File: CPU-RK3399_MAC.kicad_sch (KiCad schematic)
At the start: 15 parts, among them U1 RK3399

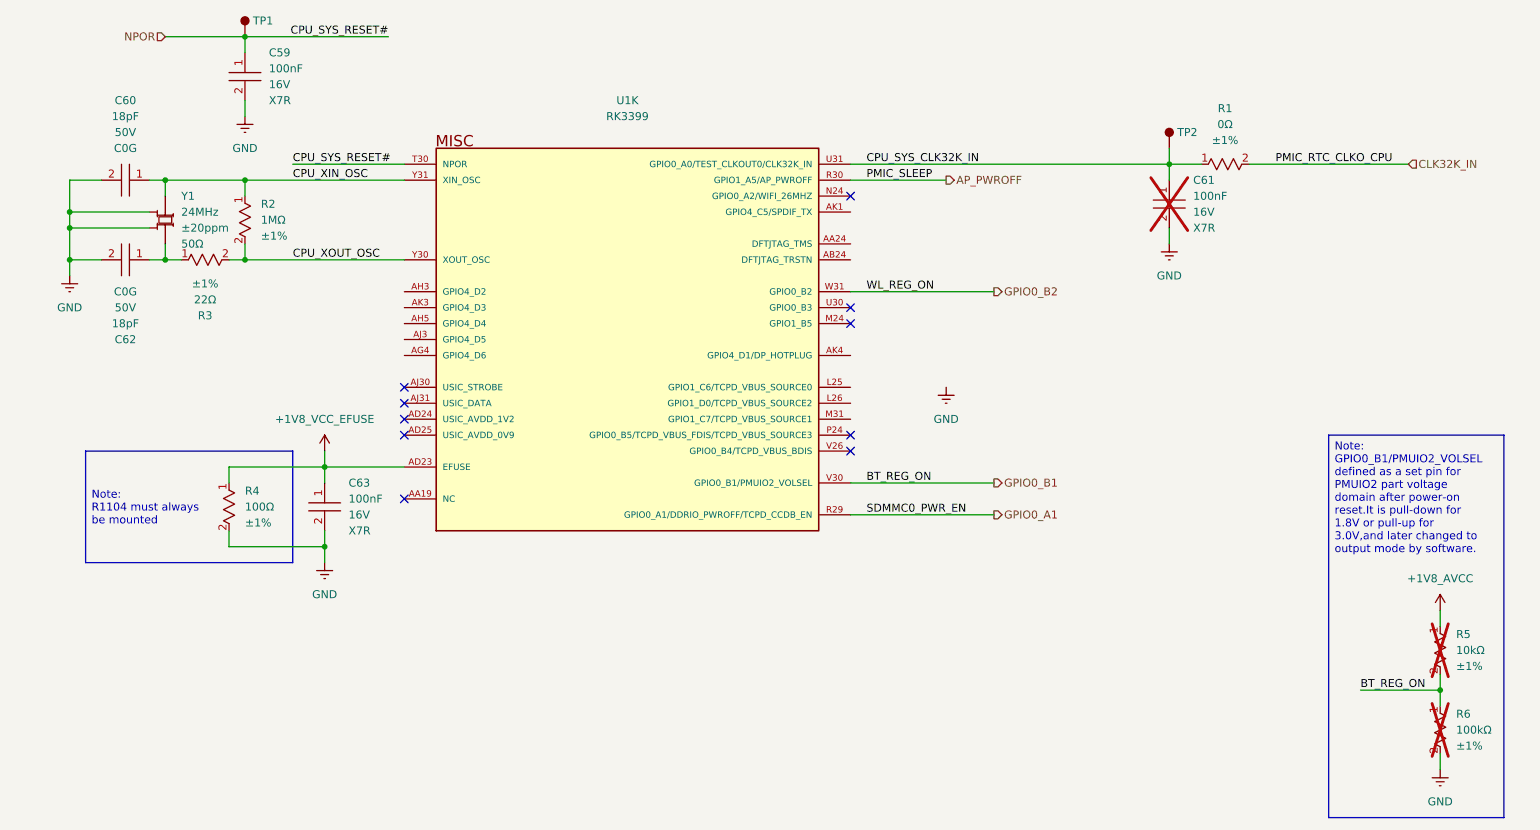
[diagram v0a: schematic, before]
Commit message: update schematic
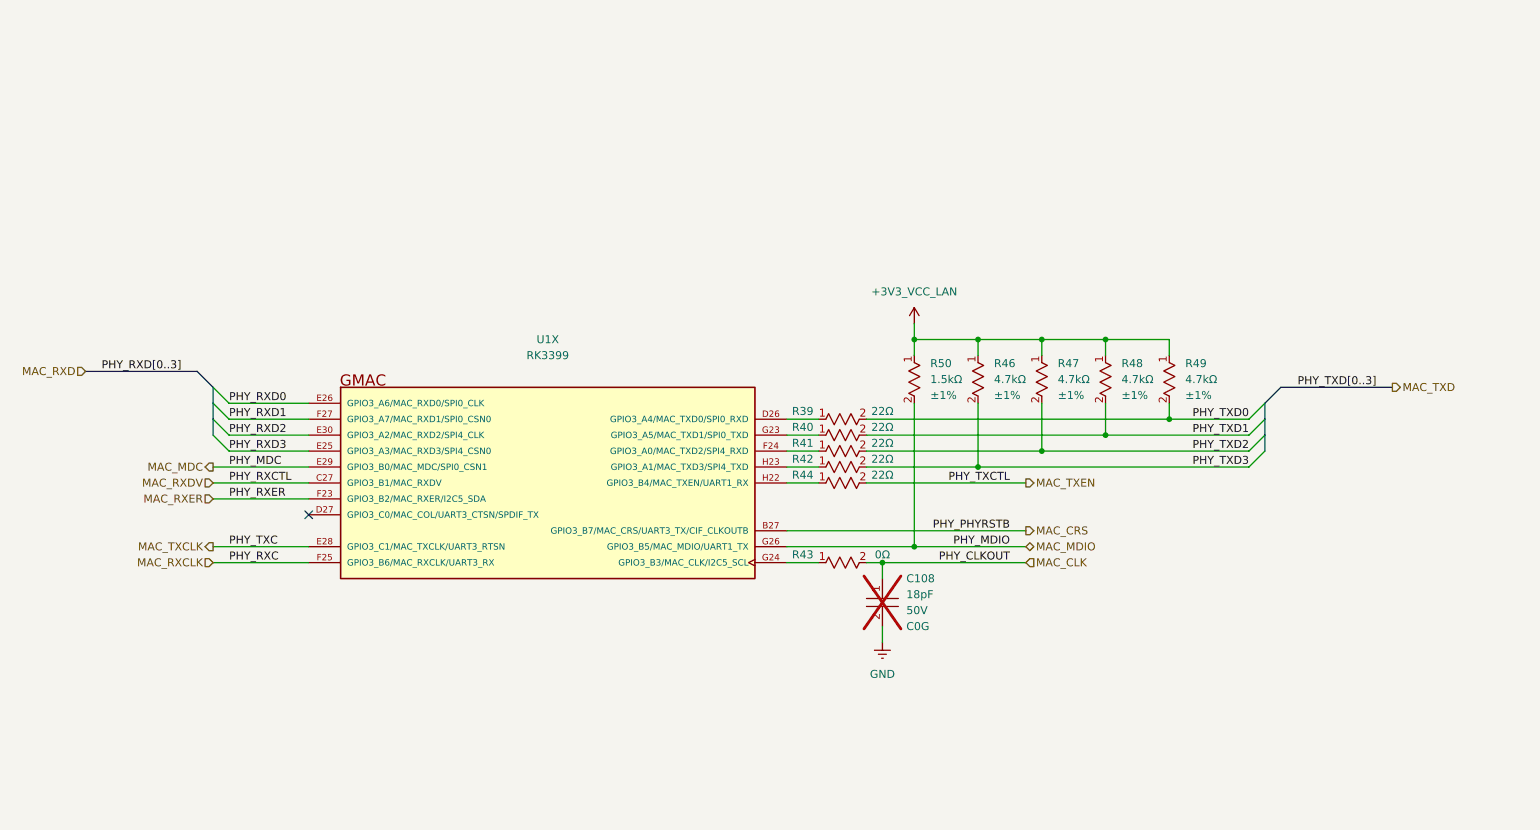
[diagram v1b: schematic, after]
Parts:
- removed C59, C61, C63: ~, footprints:CAPC1005X50N, symbol component_library:Capacitors/CL05B104KO5NNNC
- removed C60, C62: ~, footprints:CAPC1005X50N, symbol component_library:Capacitors/0402CG180J500NT
- removed R1: ~, footprints:RESC1005X35N, symbol component_library:Resistors/0402WGF0000TCE
- removed R2: ~, footprints:RESC1005X35N, symbol component_library:Resistors/0402WGF1004TCE
- removed R3: ~, footprints:RESC1005X35N, symbol component_library:Resistors/0402WGF220JTCE
- removed R4: ~, footprints:RESC1005X35N, symbol component_library:Resistors/0402WGF1000TCE
- removed R5: ~, footprints:RESC1005X35N, symbol component_library:Resistors/0402WGF1002TCE
- removed R6: ~, footprints:RESC1005X35N, symbol component_library:Resistors/0402WGF1003TCE
- removed TP1, TP2: ~, footprints:, symbol component_library:Mechanical/Test_Point
- removed U1: RK3399, footprints:BGA828C65P31X31_2100X2100X161, symbol component_library:System On Chip (SoC)/RK3399
- removed Y1: ~, footprints:, symbol component_library:Crystals, Oscillators, Resonators/X322524MOB4SI
- added C108: ~, footprints:CAPC1005X50N, symbol component_library:Capacitors/0402CG180J500NT
- added R39, R40, R41, R42, R44: ~, footprints:RESC1005X35N, symbol component_library:Resistors/0402WGF220JTCE
- added R43: ~, footprints:RESC1005X35N, symbol component_library:Resistors/0402WGF0000TCE
- added R46, R47, R48, R49: ~, footprints:RESC1005X35N, symbol component_library:Resistors/0402WGF4701TCE
- added R50: ~, footprints:RESC1005X35N, symbol component_library:Resistors/0402WGF1501TCE
- added U1: RK3399, footprints:BGA828C65P31X31_2100X2100X161, symbol component_library:System On Chip (SoC)/RK3399
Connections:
- net GND: now also C108.2
- new net: R39.1, U1.D26 (GPIO3_A4/MAC_TXD0/SPI0_RXD)
- new net: R41.1, U1.F24 (GPIO3_A0/MAC_TXD2/SPI4_RXD)
- new net: R40.1, U1.G23 (GPIO3_A5/MAC_TXD1/SPI0_TXD)
- new net: R43.1, U1.G24 (GPIO3_B3/MAC_CLK/I2C5_SCL)
- new net: R44.1, U1.H22 (GPIO3_B4/MAC_TXEN/UART1_RX)
- new net: R42.1, U1.H23 (GPIO3_A1/MAC_TXD3/SPI4_TXD)
- new net +3V3_VCC_LAN: R46.1, R47.1, R48.1, R49.1, R50.1
- new net MAC_CLK: C108.1, R43.2
- new net MAC_CRS: U1.B27 (GPIO3_B7/MAC_CRS/UART3_TX/CIF_CLKOUTB)
- new net MAC_MDC: U1.E29 (GPIO3_B0/MAC_MDC/SPI0_CSN1)
- new net MAC_MDIO: R50.2, U1.G26 (GPIO3_B5/MAC_MDIO/UART1_TX)
- new net MAC_RXCLK: U1.F25 (GPIO3_B6/MAC_RXCLK/UART3_RX)
- new net MAC_RXDV: U1.C27 (GPIO3_B1/MAC_RXDV)
- new net MAC_RXER: U1.F23 (GPIO3_B2/MAC_RXER/I2C5_SDA)
- new net MAC_TXCLK: U1.E28 (GPIO3_C1/MAC_TXCLK/UART3_RTSN)
- new net MAC_TXEN: R44.2
- new net PHY_RXD0: U1.E26 (GPIO3_A6/MAC_RXD0/SPI0_CLK)
- new net PHY_RXD1: U1.F27 (GPIO3_A7/MAC_RXD1/SPI0_CSN0)
- new net PHY_RXD2: U1.E30 (GPIO3_A2/MAC_RXD2/SPI4_CLK)
- new net PHY_RXD3: U1.E25 (GPIO3_A3/MAC_RXD3/SPI4_CSN0)
- new net PHY_TXD0: R39.2, R49.2
- new net PHY_TXD1: R40.2, R48.2
- new net PHY_TXD2: R41.2, R47.2
- new net PHY_TXD3: R42.2, R46.2
- no-connect marks 10 -> 1
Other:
- title: CPU-RK3399 PMU -> CPU-RK3399 MAC Controller

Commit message: update design power
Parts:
- renumbered C108 to C163, R50 to R62, R46 to R63, R47 to R64, R48 to R65, R49 to R66, R39 to R67, R40 to R68, R41 to R69, R42 to R70, R44 to R71, R43 to R72, U1 to U2
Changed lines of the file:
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@@
 		(dnp no)
 		(fields_autoplaced yes)
-		(property "Reference" "U1"
+		(property "Reference" "U2"
 			(at 126.998 83.82 0)
 			(effects
@@
 			(project ""
 				(path "/ebc9dc57-8b05-484a-a5cd-c53b1efc71d3/a7299b18-4123-434b-8c69-0b9524fffa12/7a7ed7e9-2984-44c5-925a-99999bacbf30"
-					(reference "U1")
+					(reference "U2")
 					(unit 24)
 				)
@@
 		(on_board yes)
 		(dnp no)
-		(property "Reference" "#PWR0122"
+		(property "Reference" "#PWR0202"
 			(at 185.42 85.09 0)
 			(effects
@@
 			(project "VESA-SBC3399"
 				(path "/ebc9dc57-8b05-484a-a5cd-c53b1efc71d3/a7299b18-4123-434b-8c69-0b9524fffa12/7a7ed7e9-2984-44c5-925a-99999bacbf30"
-					(reference "#PWR0122")
+					(reference "#PWR0202")
 					(unit 1)
 				)
@@
 		(dnp no)
 		(fields_autoplaced yes)
-		(property "Reference" "R50"
+		(property "Reference" "R62"
 			(at 187.96 87.6299 90)
 			(effects
@@
 			(project ""
 				(path "/ebc9dc57-8b05-484a-a5cd-c53b1efc71d3/a7299b18-4123-434b-8c69-0b9524fffa12/7a7ed7e9-2984-44c5-925a-99999bacbf30"
-					(reference "R50")
+					(reference "R62")
 					(unit 1)
 				)
@@
 		(dnp no)
 		(fields_autoplaced yes)
-		(property "Reference" "R46"
+		(property "Reference" "R63"
 			(at 198.12 87.6299 90)
 			(effects
@@
 			(project ""
 				(path "/ebc9dc57-8b05-484a-a5cd-c53b1efc71d3/a7299b18-4123-434b-8c69-0b9524fffa12/7a7ed7e9-2984-44c5-925a-99999bacbf30"
-					(reference "R46")
+					(reference "R63")
 					(unit 1)
 				)
@@
 		(dnp no)
 		(fields_autoplaced yes)
-		(property "Reference" "R47"
+		(property "Reference" "R64"
 			(at 208.28 87.6299 90)
 			(effects
@@
 			(project "VESA-SBC3399"
 				(path "/ebc9dc57-8b05-484a-a5cd-c53b1efc71d3/a7299b18-4123-434b-8c69-0b9524fffa12/7a7ed7e9-2984-44c5-925a-99999bacbf30"
-					(reference "R47")
+					(reference "R64")
 					(unit 1)
 				)
@@
 		(on_board yes)
 		(dnp no)
-		(property "Reference" "R39"
+		(property "Reference" "R67"
 			(at 167.64 95.25 0)
 			(effects
@@
 			(project ""
 				(path "/ebc9dc57-8b05-484a-a5cd-c53b1efc71d3/a7299b18-4123-434b-8c69-0b9524fffa12/7a7ed7e9-2984-44c5-925a-99999bacbf30"
-					(reference "R39")
+					(reference "R67")
 					(unit 1)
 				)
@@
 		(on_board yes)
 		(dnp no)
-		(property "Reference" "R42"
+		(property "Reference" "R70"
 			(at 167.64 102.87 0)
 			(effects
@@
 			(project "VESA-SBC3399"
 				(path "/ebc9dc57-8b05-484a-a5cd-c53b1efc71d3/a7299b18-4123-434b-8c69-0b9524fffa12/7a7ed7e9-2984-44c5-925a-99999bacbf30"
-					(reference "R42")
+					(reference "R70")
 					(unit 1)
 				)
@@
 		(on_board yes)
 		(dnp no)
-		(property "Reference" "R43"
+		(property "Reference" "R72"
 			(at 167.64 118.11 0)
 			(effects
@@
 			(project "VESA-SBC3399"
 				(path "/ebc9dc57-8b05-484a-a5cd-c53b1efc71d3/a7299b18-4123-434b-8c69-0b9524fffa12/7a7ed7e9-2984-44c5-925a-99999bacbf30"
-					(reference "R43")
+					(reference "R72")
 					(unit 1)
 				)
@@
 		(on_board yes)
 		(dnp no)
-		(property "Reference" "R41"
+		(property "Reference" "R69"
 			(at 167.64 100.33 0)
 			(effects
@@
 			(project "VESA-SBC3399"
 				(path "/ebc9dc57-8b05-484a-a5cd-c53b1efc71d3/a7299b18-4123-434b-8c69-0b9524fffa12/7a7ed7e9-2984-44c5-925a-99999bacbf30"
-					(reference "R41")
+					(reference "R69")
 					(unit 1)
 				)
@@
 		(on_board yes)
 		(dnp no)
-		(property "Reference" "R40"
+		(property "Reference" "R68"
 			(at 167.64 97.79 0)
 			(effects
@@
 			(project "VESA-SBC3399"
 				(path "/ebc9dc57-8b05-484a-a5cd-c53b1efc71d3/a7299b18-4123-434b-8c69-0b9524fffa12/7a7ed7e9-2984-44c5-925a-99999bacbf30"
-					(reference "R40")
+					(reference "R68")
 					(unit 1)
 				)
@@
 		(dnp no)
 		(fields_autoplaced yes)
-		(property "Reference" "R49"
+		(property "Reference" "R66"
 			(at 228.6 87.6299 90)
 			(effects
@@
 			(project "VESA-SBC3399"
 				(path "/ebc9dc57-8b05-484a-a5cd-c53b1efc71d3/a7299b18-4123-434b-8c69-0b9524fffa12/7a7ed7e9-2984-44c5-925a-99999bacbf30"
-					(reference "R49")
+					(reference "R66")
 					(unit 1)
 				)
@@
 		(on_board yes)
 		(dnp no)
-		(property "Reference" "R44"
+		(property "Reference" "R71"
 			(at 167.64 105.41 0)
 			(effects
@@
 			(project "VESA-SBC3399"
 				(path "/ebc9dc57-8b05-484a-a5cd-c53b1efc71d3/a7299b18-4123-434b-8c69-0b9524fffa12/7a7ed7e9-2984-44c5-925a-99999bacbf30"
-					(reference "R44")
+					(reference "R71")
 					(unit 1)
 				)
@@
 		(dnp no)
 		(fields_autoplaced yes)
-		(property "Reference" "#PWR0115"
+		(property "Reference" "#PWR0203"
 			(at 180.34 138.43 0)
 			(effects
@@
 			(project "VESA-SBC3399"
 				(path "/ebc9dc57-8b05-484a-a5cd-c53b1efc71d3/a7299b18-4123-434b-8c69-0b9524fffa12/7a7ed7e9-2984-44c5-925a-99999bacbf30"
-					(reference "#PWR0115")
+					(reference "#PWR0203")
 					(unit 1)
 				)
@@
 		(dnp no)
 		(fields_autoplaced yes)
-		(property "Reference" "R48"
+		(property "Reference" "R65"
 			(at 218.44 87.6299 90)
 			(effects
@@
 			(project "VESA-SBC3399"
 				(path "/ebc9dc57-8b05-484a-a5cd-c53b1efc71d3/a7299b18-4123-434b-8c69-0b9524fffa12/7a7ed7e9-2984-44c5-925a-99999bacbf30"
-					(reference "R48")
+					(reference "R65")
 					(unit 1)
 				)
@@
 		(on_board yes)
 		(dnp yes)
-		(property "Reference" "C108"
+		(property "Reference" "C163"
 			(at 184.15 121.9199 0)
 			(effects
@@
 			(project "VESA-SBC3399"
 				(path "/ebc9dc57-8b05-484a-a5cd-c53b1efc71d3/a7299b18-4123-434b-8c69-0b9524fffa12/7a7ed7e9-2984-44c5-925a-99999bacbf30"
-					(reference "C108")
+					(reference "C163")
 					(unit 1)
 				)

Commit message: design DDR
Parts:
- renumbered C163 to C290, R62 to R133, R63 to R134, R64 to R135, R65 to R136, R66 to R137, R67 to R138, R68 to R139, R69 to R140, R70 to R141, R71 to R142, R72 to R143, U2 to U17
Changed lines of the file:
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@@
 		(dnp no)
 		(fields_autoplaced yes)
-		(property "Reference" "U2"
+		(property "Reference" "U17"
 			(at 126.998 83.82 0)
 			(effects
@@
 		)
 		(property "Footprint" "footprints:BGA828C65P31X31_2100X2100X161"
-			(at 129.54 109.22 0)
+			(at 127 109.22 0)
 			(effects
 				(font
@@
 			(project ""
 				(path "/ebc9dc57-8b05-484a-a5cd-c53b1efc71d3/a7299b18-4123-434b-8c69-0b9524fffa12/7a7ed7e9-2984-44c5-925a-99999bacbf30"
-					(reference "U2")
+					(reference "U17")
 					(unit 24)
 				)
@@
 		(on_board yes)
 		(dnp no)
-		(property "Reference" "#PWR0202"
+		(property "Reference" "#PWR0362"
 			(at 185.42 85.09 0)
 			(effects
@@
 			(project "VESA-SBC3399"
 				(path "/ebc9dc57-8b05-484a-a5cd-c53b1efc71d3/a7299b18-4123-434b-8c69-0b9524fffa12/7a7ed7e9-2984-44c5-925a-99999bacbf30"
-					(reference "#PWR0202")
+					(reference "#PWR0362")
 					(unit 1)
 				)
@@
 		(dnp no)
 		(fields_autoplaced yes)
-		(property "Reference" "R62"
+		(property "Reference" "R133"
 			(at 187.96 87.6299 90)
 			(effects
@@
 			(project ""
 				(path "/ebc9dc57-8b05-484a-a5cd-c53b1efc71d3/a7299b18-4123-434b-8c69-0b9524fffa12/7a7ed7e9-2984-44c5-925a-99999bacbf30"
-					(reference "R62")
+					(reference "R133")
 					(unit 1)
 				)
@@
 		(dnp no)
 		(fields_autoplaced yes)
-		(property "Reference" "R63"
+		(property "Reference" "R134"
 			(at 198.12 87.6299 90)
 			(effects
@@
 			(project ""
 				(path "/ebc9dc57-8b05-484a-a5cd-c53b1efc71d3/a7299b18-4123-434b-8c69-0b9524fffa12/7a7ed7e9-2984-44c5-925a-99999bacbf30"
-					(reference "R63")
+					(reference "R134")
 					(unit 1)
 				)
@@
 		(dnp no)
 		(fields_autoplaced yes)
-		(property "Reference" "R64"
+		(property "Reference" "R135"
 			(at 208.28 87.6299 90)
 			(effects
@@
 			(project "VESA-SBC3399"
 				(path "/ebc9dc57-8b05-484a-a5cd-c53b1efc71d3/a7299b18-4123-434b-8c69-0b9524fffa12/7a7ed7e9-2984-44c5-925a-99999bacbf30"
-					(reference "R64")
+					(reference "R135")
 					(unit 1)
 				)
@@
 		(on_board yes)
 		(dnp no)
-		(property "Reference" "R67"
+		(property "Reference" "R138"
 			(at 167.64 95.25 0)
 			(effects
@@
 			(project ""
 				(path "/ebc9dc57-8b05-484a-a5cd-c53b1efc71d3/a7299b18-4123-434b-8c69-0b9524fffa12/7a7ed7e9-2984-44c5-925a-99999bacbf30"
-					(reference "R67")
+					(reference "R138")
 					(unit 1)
 				)
@@
 		(on_board yes)
 		(dnp no)
-		(property "Reference" "R70"
+		(property "Reference" "R141"
 			(at 167.64 102.87 0)
 			(effects
@@
 			(project "VESA-SBC3399"
 				(path "/ebc9dc57-8b05-484a-a5cd-c53b1efc71d3/a7299b18-4123-434b-8c69-0b9524fffa12/7a7ed7e9-2984-44c5-925a-99999bacbf30"
-					(reference "R70")
+					(reference "R141")
 					(unit 1)
 				)
@@
 		(on_board yes)
 		(dnp no)
-		(property "Reference" "R72"
+		(property "Reference" "R143"
 			(at 167.64 118.11 0)
 			(effects
@@
 			(project "VESA-SBC3399"
 				(path "/ebc9dc57-8b05-484a-a5cd-c53b1efc71d3/a7299b18-4123-434b-8c69-0b9524fffa12/7a7ed7e9-2984-44c5-925a-99999bacbf30"
-					(reference "R72")
+					(reference "R143")
 					(unit 1)
 				)
@@
 		(on_board yes)
 		(dnp no)
-		(property "Reference" "R69"
+		(property "Reference" "R140"
 			(at 167.64 100.33 0)
 			(effects
@@
 			(project "VESA-SBC3399"
 				(path "/ebc9dc57-8b05-484a-a5cd-c53b1efc71d3/a7299b18-4123-434b-8c69-0b9524fffa12/7a7ed7e9-2984-44c5-925a-99999bacbf30"
-					(reference "R69")
+					(reference "R140")
 					(unit 1)
 				)
@@
 		(on_board yes)
 		(dnp no)
-		(property "Reference" "R68"
+		(property "Reference" "R139"
 			(at 167.64 97.79 0)
 			(effects
@@
 			(project "VESA-SBC3399"
 				(path "/ebc9dc57-8b05-484a-a5cd-c53b1efc71d3/a7299b18-4123-434b-8c69-0b9524fffa12/7a7ed7e9-2984-44c5-925a-99999bacbf30"
-					(reference "R68")
+					(reference "R139")
 					(unit 1)
 				)
@@
 		(dnp no)
 		(fields_autoplaced yes)
-		(property "Reference" "R66"
+		(property "Reference" "R137"
 			(at 228.6 87.6299 90)
 			(effects
@@
 			(project "VESA-SBC3399"
 				(path "/ebc9dc57-8b05-484a-a5cd-c53b1efc71d3/a7299b18-4123-434b-8c69-0b9524fffa12/7a7ed7e9-2984-44c5-925a-99999bacbf30"
-					(reference "R66")
+					(reference "R137")
 					(unit 1)
 				)
@@
 		(on_board yes)
 		(dnp no)
-		(property "Reference" "R71"
+		(property "Reference" "R142"
 			(at 167.64 105.41 0)
 			(effects
@@
 			(project "VESA-SBC3399"
 				(path "/ebc9dc57-8b05-484a-a5cd-c53b1efc71d3/a7299b18-4123-434b-8c69-0b9524fffa12/7a7ed7e9-2984-44c5-925a-99999bacbf30"
-					(reference "R71")
+					(reference "R142")
 					(unit 1)
 				)
@@
 		(dnp no)
 		(fields_autoplaced yes)
-		(property "Reference" "#PWR0203"
+		(property "Reference" "#PWR0363"
 			(at 180.34 138.43 0)
 			(effects
@@
 			(project "VESA-SBC3399"
 				(path "/ebc9dc57-8b05-484a-a5cd-c53b1efc71d3/a7299b18-4123-434b-8c69-0b9524fffa12/7a7ed7e9-2984-44c5-925a-99999bacbf30"
-					(reference "#PWR0203")
+					(reference "#PWR0363")
 					(unit 1)
 				)
@@
 		(dnp no)
 		(fields_autoplaced yes)
-		(property "Reference" "R65"
+		(property "Reference" "R136"
 			(at 218.44 87.6299 90)
 			(effects
@@
 			(project "VESA-SBC3399"
 				(path "/ebc9dc57-8b05-484a-a5cd-c53b1efc71d3/a7299b18-4123-434b-8c69-0b9524fffa12/7a7ed7e9-2984-44c5-925a-99999bacbf30"
-					(reference "R65")
+					(reference "R136")
 					(unit 1)
 				)
@@
 		(on_board yes)
 		(dnp yes)
-		(property "Reference" "C163"
+		(property "Reference" "C290"
 			(at 184.15 121.9199 0)
 			(effects
@@
 			(project "VESA-SBC3399"
 				(path "/ebc9dc57-8b05-484a-a5cd-c53b1efc71d3/a7299b18-4123-434b-8c69-0b9524fffa12/7a7ed7e9-2984-44c5-925a-99999bacbf30"
-					(reference "C163")
+					(reference "C290")
 					(unit 1)
 				)
